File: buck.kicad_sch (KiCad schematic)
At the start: 17 parts, among them IC3 LM5085MY_NOPB, Q3 PMOS

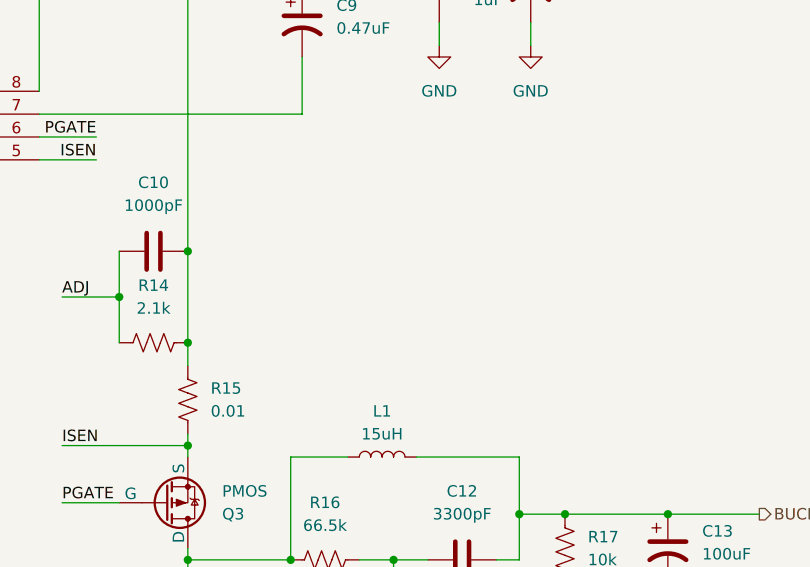
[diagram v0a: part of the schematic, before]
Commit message: added logic level translator
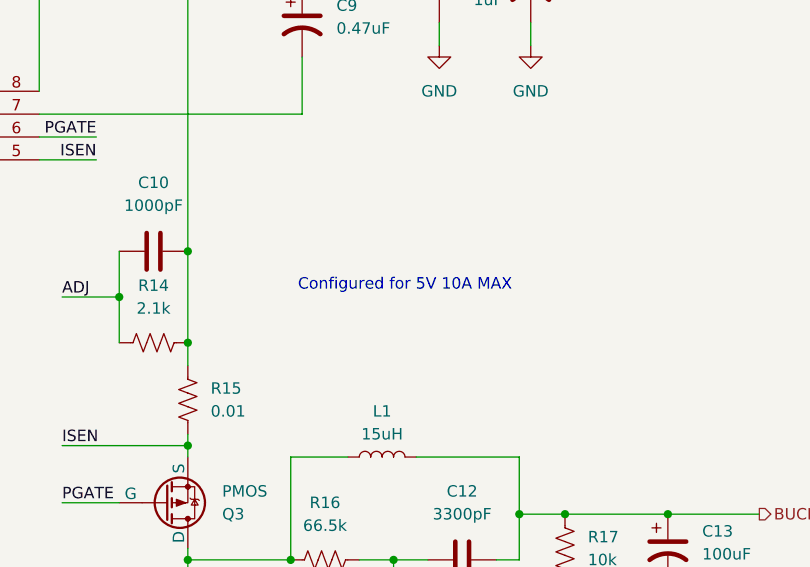
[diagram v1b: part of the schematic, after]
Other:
- note added: "Configured for 5V 10A MAX"
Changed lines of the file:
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@@
+		)
+	)
+	(text "Configured for 5V 10A MAX"
+		(exclude_from_sim no)
+		(at 187.96 107.95 0)
+		(effects
+			(font
+				(size 1.27 1.27)
+			)
 		)
 	)
 	(label "ADJ"
 		(at 113.03 86.36 0)
-		(fields_autoplaced yes)
 		(effects
 			(font
@@
 	(label "ISEN"
 		(at 149.86 125.73 0)
-		(fields_autoplaced yes)
 		(effects
 			(font
@@
 	(label "FB"
 		(at 113.03 91.44 0)
-		(fields_autoplaced yes)
 		(effects
 			(font
@@
 	(label "PGATE"
 		(at 149.86 132.08 0)
-		(fields_autoplaced yes)
 		(effects
 			(font
@@
 	(label "ISEN"
 		(at 153.67 93.98 180)
-		(fields_autoplaced yes)
 		(effects
 			(font
@@
 	(label "FB"
 		(at 180.34 148.59 0)
-		(fields_autoplaced yes)
 		(effects
 			(font
@@
 	(label "PGATE"
 		(at 153.67 91.44 180)
-		(fields_autoplaced yes)
 		(effects
 			(font
@@
 	(label "ADJ"
 		(at 149.86 109.22 0)
-		(fields_autoplaced yes)
 		(effects
 			(font
@@
 		(shape input)
 		(at 204.47 71.12 0)
-		(fields_autoplaced yes)
 		(effects
 			(font
@@
 		(shape output)
 		(at 227.33 133.35 0)
-		(fields_autoplaced yes)
 		(effects
 			(font
@@
 		(shape input)
 		(at 100.33 80.01 180)
-		(fields_autoplaced yes)
 		(effects
 			(font
@@
 		(shape input)
 		(at 111.76 93.98 180)
-		(fields_autoplaced yes)
 		(effects
 			(font

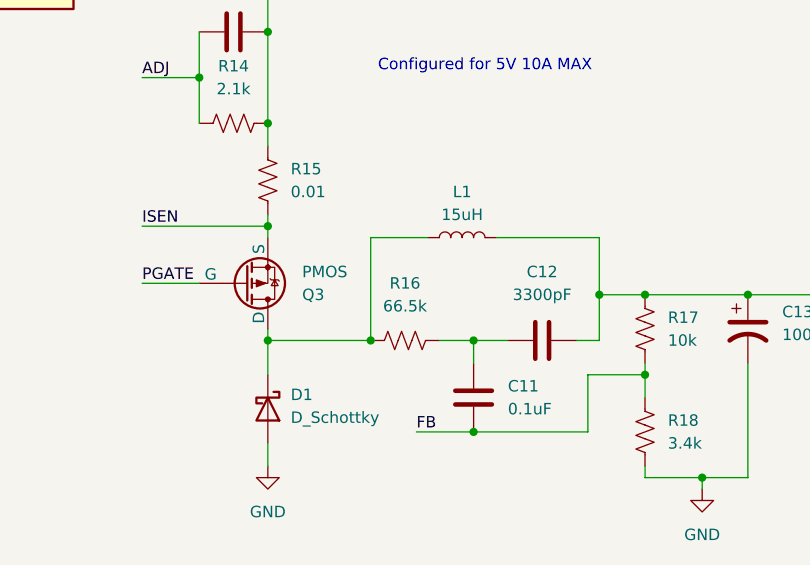
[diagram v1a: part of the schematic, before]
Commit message: added screen and gpio buttons
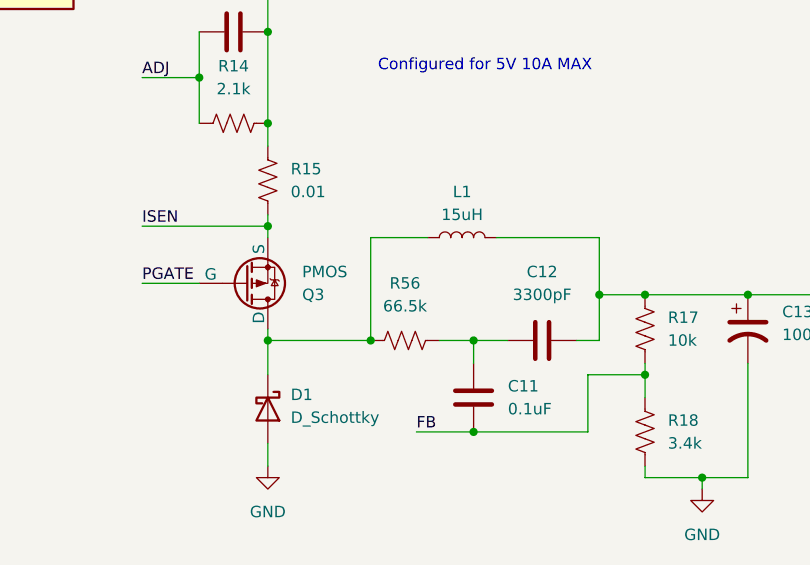
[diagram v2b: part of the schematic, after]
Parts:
- renumbered R16 to R56
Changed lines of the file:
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@@
 		(dnp no)
 		(fields_autoplaced yes)
-		(property "Reference" "R16"
+		(property "Reference" "R56"
 			(at 179.07 132.08 90)
 			(effects
@@
 			(project "Cell-Characterization-Board"
 				(path "/8cf78a1b-eb7a-4166-aa75-ad898a030304/02e804c2-1162-421a-8f6e-0436cbda7935/6dd76b9e-36b5-4388-b4ca-2270a7f63132"
-					(reference "R16")
+					(reference "R56")
 					(unit 1)
 				)

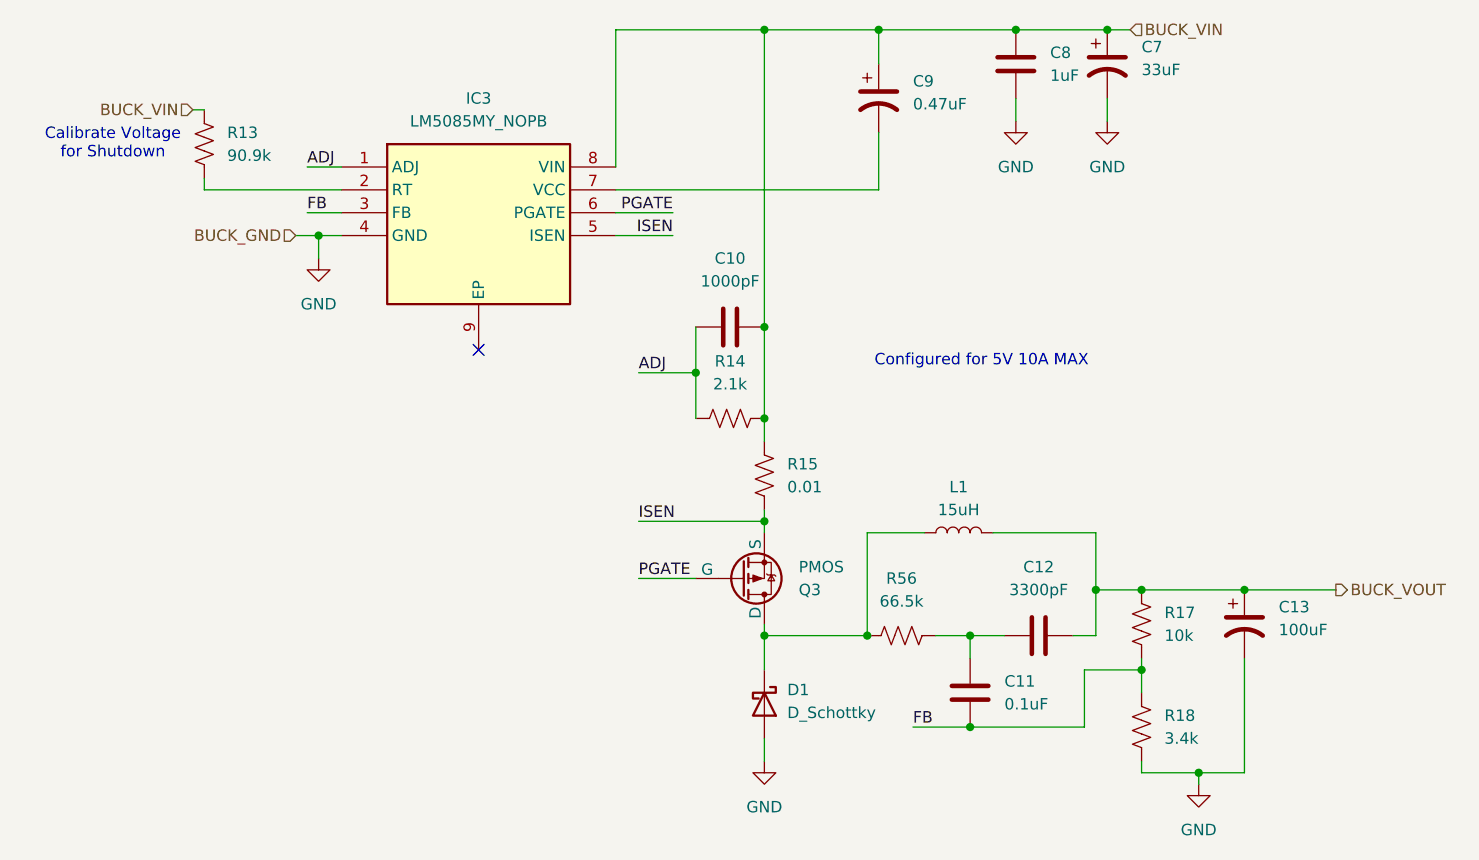
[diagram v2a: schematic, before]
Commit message: Updated current control loop hardware
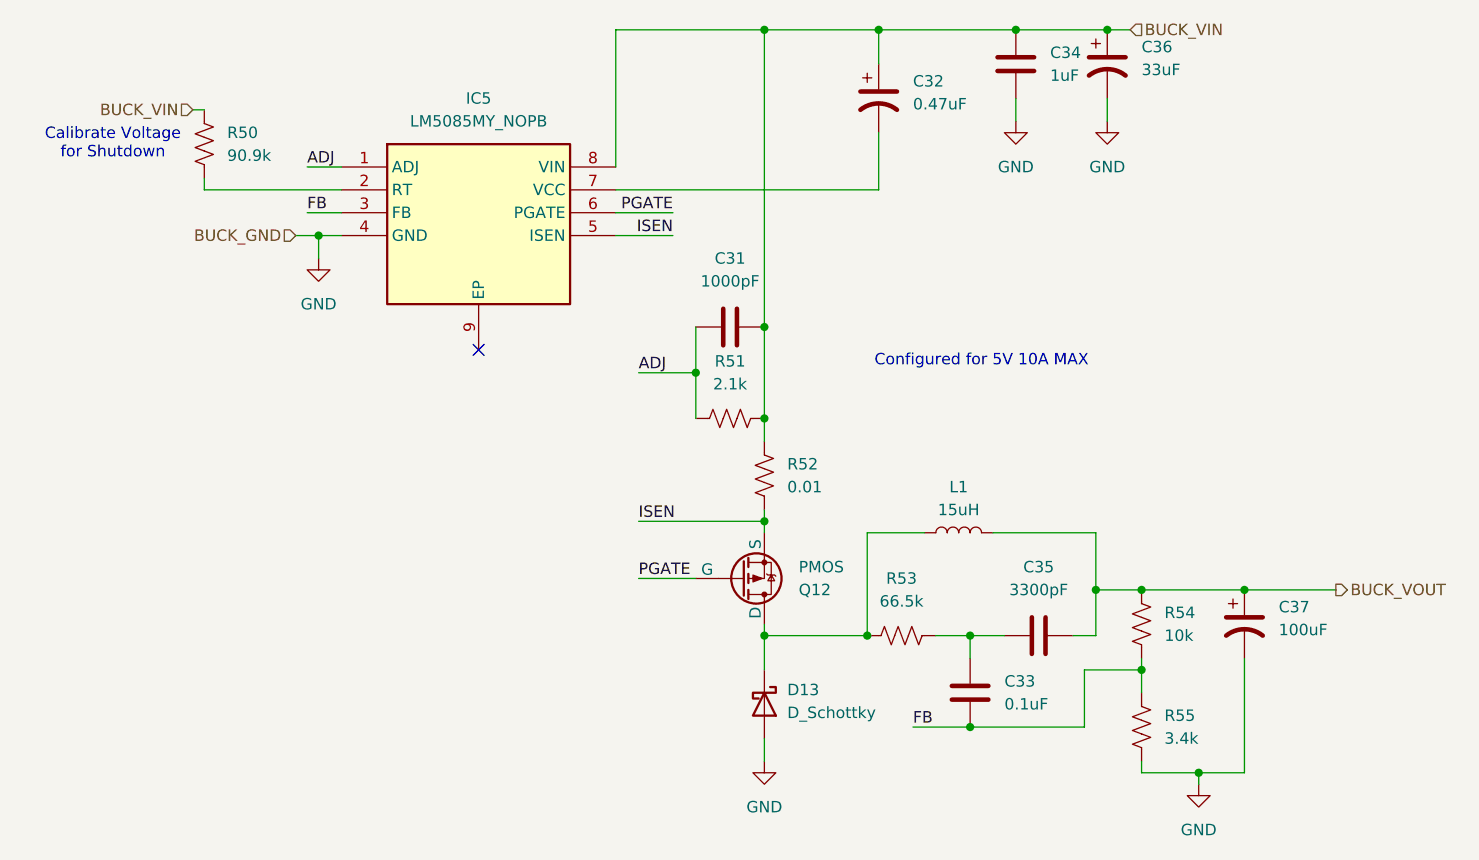
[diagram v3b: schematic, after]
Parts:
- removed C13: 100uF, symbol Device:C_Polarized_US
- added C37: 100uF, symbol Device:C_Polarized_US
- renumbered C10 to C31, C9 to C32, C11 to C33, C8 to C34, C12 to C35, C7 to C36, D1 to D13, IC3 to IC5, Q3 to Q12, R13 to R50, R14 to R51, R15 to R52, R56 to R53, R17 to R54, R18 to R55
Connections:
- net BUCK_VOUT: now also C37.1
- net GND: now also C37.2

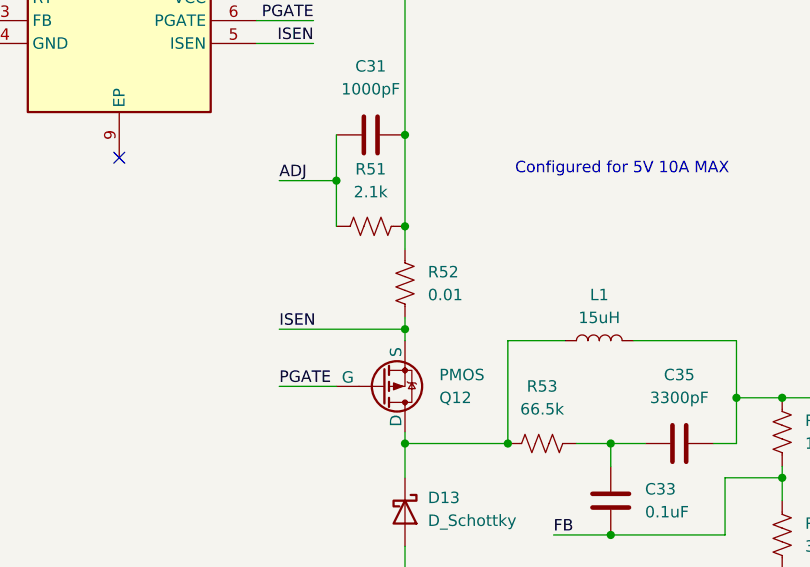
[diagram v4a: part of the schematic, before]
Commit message: footprints and components for buck and power
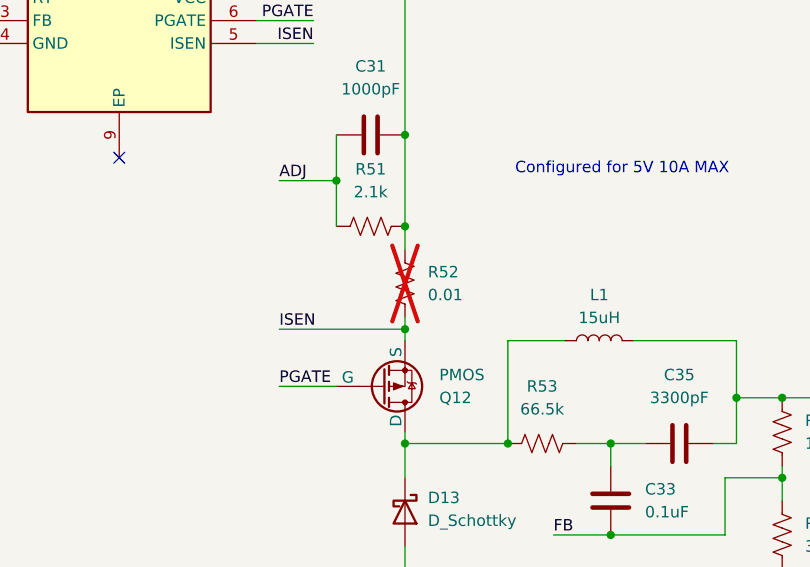
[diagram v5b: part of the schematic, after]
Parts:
- C31, C33, C34, C35: footprint (none) -> Capacitor_SMD:C_0805_2012Metric
- C32: footprint (none) -> Capacitor_SMD:C_1206_3216Metric
- C36, C37: footprint (none) -> ExternalFootprints:CAPPM7343X310N
- D13: footprint (none) -> ExternalFootprints:YQ30NL10SEFHTL
- L1: footprint (none) -> ExternalFootprints:PQ2617BHA150K
- Q12: footprint (none) -> ExternalFootprints:SOIC127P600X175-8N
- R50, R51, R53, R54, R55: footprint (none) -> Resistor_SMD:R_0805_2012Metric
- R52: footprint (none) -> Resistor_SMD:R_0805_2012Metric; now not fitted
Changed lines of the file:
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@@
 			)
 		)
-		(property "Footprint" ""
+		(property "Footprint" "Capacitor_SMD:C_0805_2012Metric"
 			(at 163.83 103.1748 0)
 			(effects
@@
 			)
 		)
-		(property "Footprint" ""
+		(property "Footprint" "Capacitor_SMD:C_0805_2012Metric"
 			(at 198.12 137.4648 0)
 			(effects
@@
 			)
 		)
-		(property "Footprint" ""
+		(property "Footprint" "ExternalFootprints:SOIC127P600X175-8N"
 			(at 166.37 134.62 0)
 			(effects
@@
 			)
 		)
-		(property "Datasheet" "https://ngspice.sourceforge.io/docs/ngspice-html-manual/manual.xhtml#cha_MOSFETs"
+		(property "Datasheet" "https://www.vishay.com/docs/67335/si4463cd.pdf"
 			(at 161.29 119.38 0)
 			(effects
@@
 			)
 		)
-		(property "Footprint" ""
+		(property "Footprint" "Resistor_SMD:R_0805_2012Metric"
 			(at 206.756 148.844 90)
 			(effects
@@
 			)
 		)
-		(property "Footprint" ""
+		(property "Footprint" "ExternalFootprints:CAPPM7343X310N"
 			(at 217.17 137.16 0)
 			(effects
@@
 			)
 		)
-		(property "Footprint" ""
+		(property "Footprint" "Resistor_SMD:R_0805_2012Metric"
 			(at 206.756 137.414 90)
 			(effects
@@
 			)
 		)
-		(property "Footprint" ""
+		(property "Footprint" "Resistor_SMD:R_0805_2012Metric"
 			(at 102.616 84.074 90)
 			(effects
@@
 			)
 		)
-		(property "Footprint" ""
+		(property "Footprint" "Resistor_SMD:R_0805_2012Metric"
 			(at 178.816 139.446 90)
 			(effects
@@
 			)
 		)
-		(property "Footprint" ""
+		(property "Footprint" "Capacitor_SMD:C_1206_3216Metric"
 			(at 176.53 78.74 0)
 			(effects
@@
 			)
 		)
-		(property "Footprint" ""
+		(property "Footprint" "Resistor_SMD:R_0805_2012Metric"
 			(at 160.274 113.284 90)
 			(effects
@@
 			)
 		)
-		(property "Footprint" ""
+		(property "Footprint" "Capacitor_SMD:C_0805_2012Metric"
 			(at 187.6552 148.59 0)
 			(effects
@@
 			)
 		)
-		(property "Footprint" ""
+		(property "Footprint" "Capacitor_SMD:C_0805_2012Metric"
 			(at 192.7352 78.74 0)
 			(effects
@@
 			)
 		)
-		(property "Footprint" ""
+		(property "Footprint" "ExternalFootprints:YQ30NL10SEFHTL"
 			(at 163.83 146.05 0)
 			(effects
@@
 			)
 		)
-		(property "Footprint" ""
+		(property "Footprint" "ExternalFootprints:PQ2617BHA150K"
 			(at 185.42 127 0)
 			(effects
@@
 			)
 		)
-		(property "Datasheet" "~"
+		(property "Datasheet" "https://www.mouser.com/datasheet/2/54/bourns_PQ2617BHA_datasheet-1159314.pdf"
 			(at 185.42 127 0)
 			(effects
@@
 			)
 		)
-		(property "Footprint" ""
+		(property "Footprint" "ExternalFootprints:CAPPM7343X310N"
 			(at 201.93 74.93 0)
 			(effects
@@
 		(in_bom yes)
 		(on_board yes)
-		(dnp no)
+		(dnp yes)
 		(fields_autoplaced yes)
 		(property "Reference" "R52"
@@
 			)
 		)
-		(property "Footprint" ""
+		(property "Footprint" "Resistor_SMD:R_0805_2012Metric"
 			(at 164.846 120.904 90)
 			(effects
